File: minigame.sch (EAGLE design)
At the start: 44 parts, among them J1 AVR_SPI_PRG_6PTH, Q1 MMBT2222A, U1 MCP73831, U2 MIC5219 3.3V, Y1 8MHz

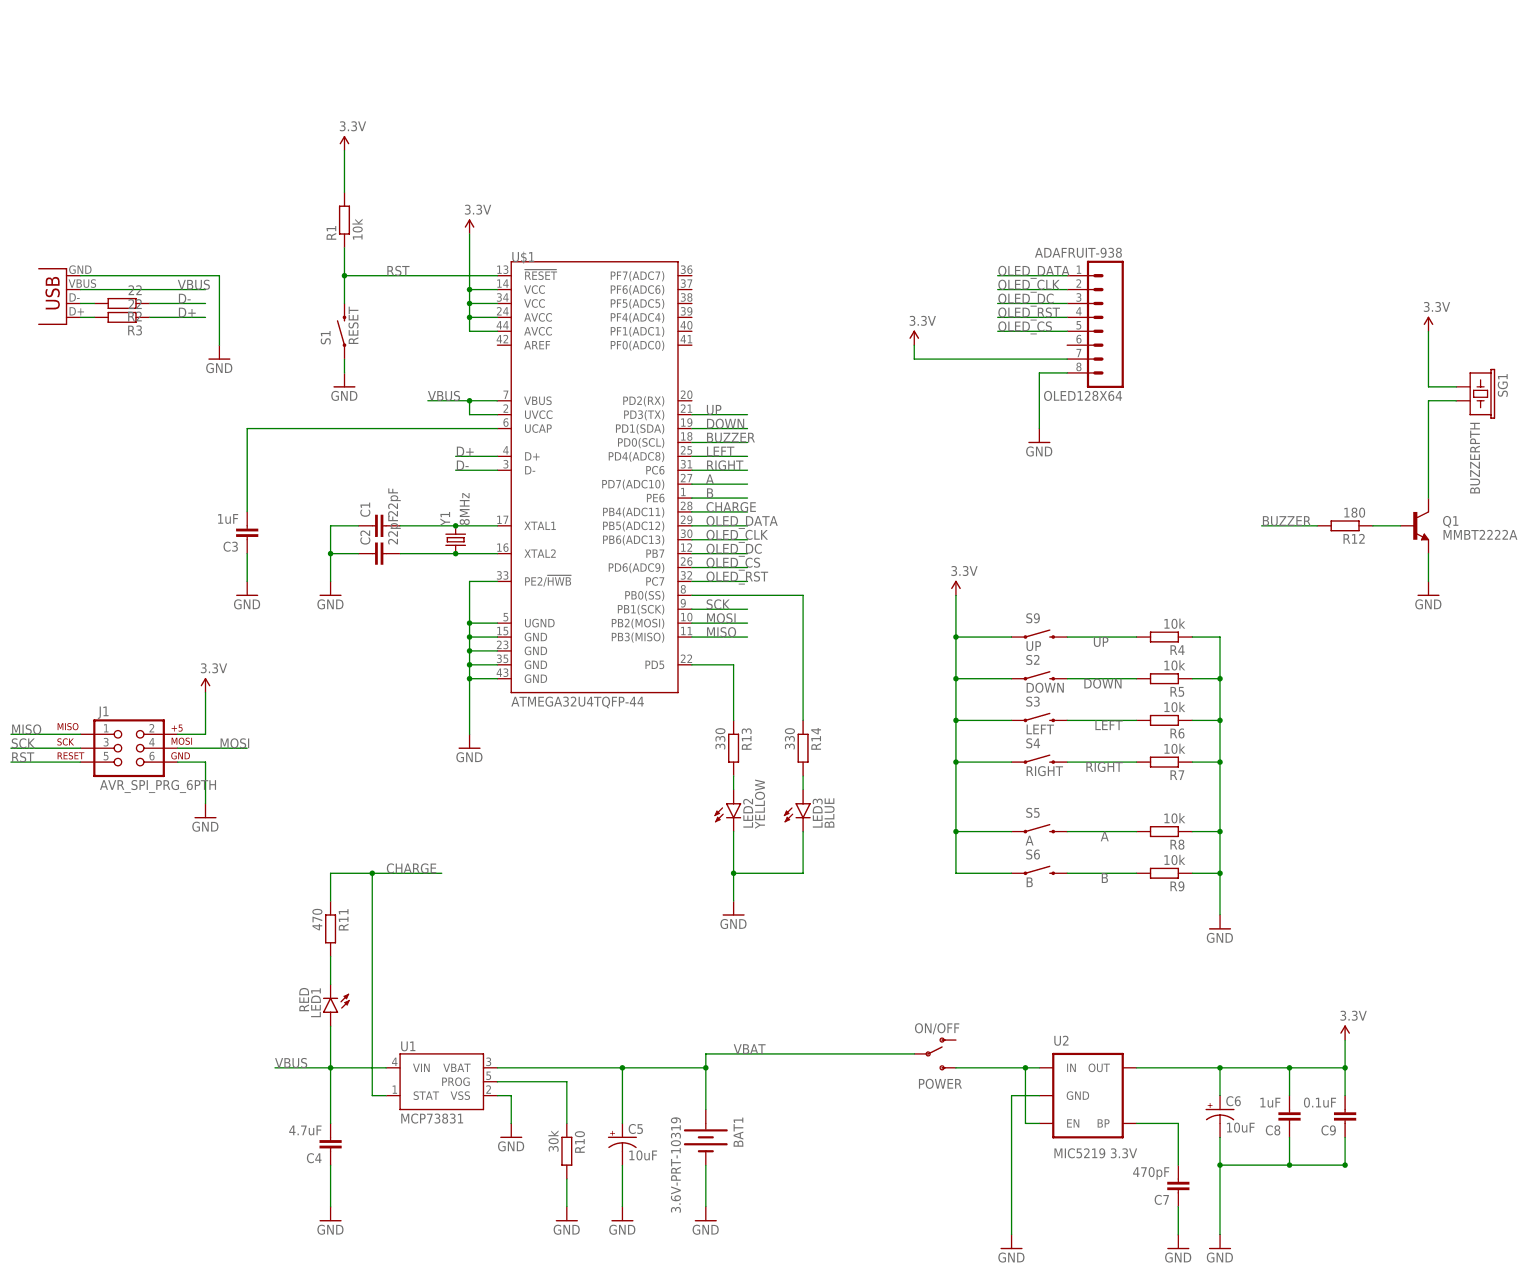
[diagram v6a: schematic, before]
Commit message: Voltage regulator removed Preliminary Routing test
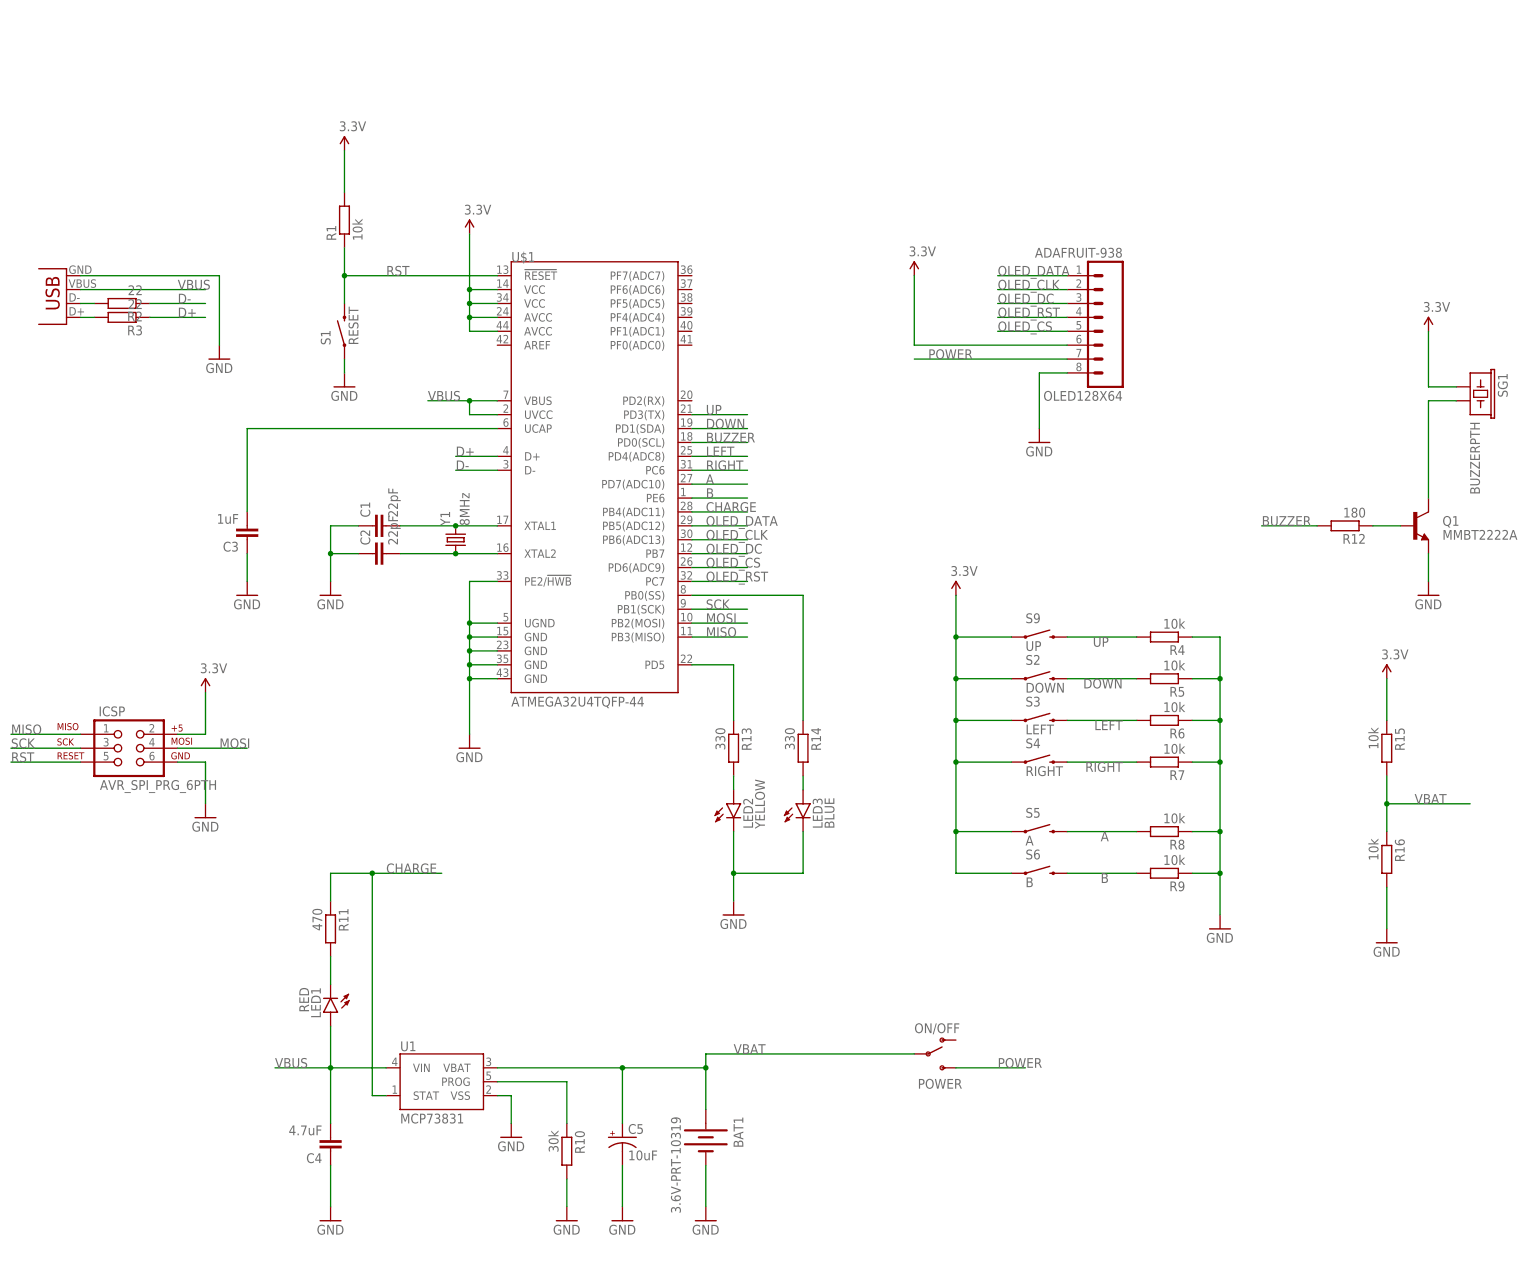
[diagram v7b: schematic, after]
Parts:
- removed C6: 10uF, SparkFun-Capacitors:CAP_POLD
- removed C7: 470pF, SparkFun-Passives:CAP1206
- removed C8: 1uF, SparkFun-Passives:CAP1206
- removed C9: 0.1uF, SparkFun-Passives:CAP1206
- removed U2: MIC5219 3.3V, SparkFun-PowerIC:V_REG_MIC52193.3V
- added R15, R16: 10k, rcl:R-EU_M0805
- renumbered J1 to ICSP
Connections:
- removed net N$10: POWER.S, U2.EN, U2.IN
- removed net N$8: C7.2, U2.BP
- new net POWER: OLED128X64.7, POWER.S
- net 3.3V: now also OLED128X64.6, R15.1; no longer C6.+, C8.2, C9.2, OLED128X64.7, U2.OUT
- net GND: now also R16.2; no longer C6.-, C7.1, C8.1, C9.1, U2.GND
- net VBAT: now also R15.2, R16.1

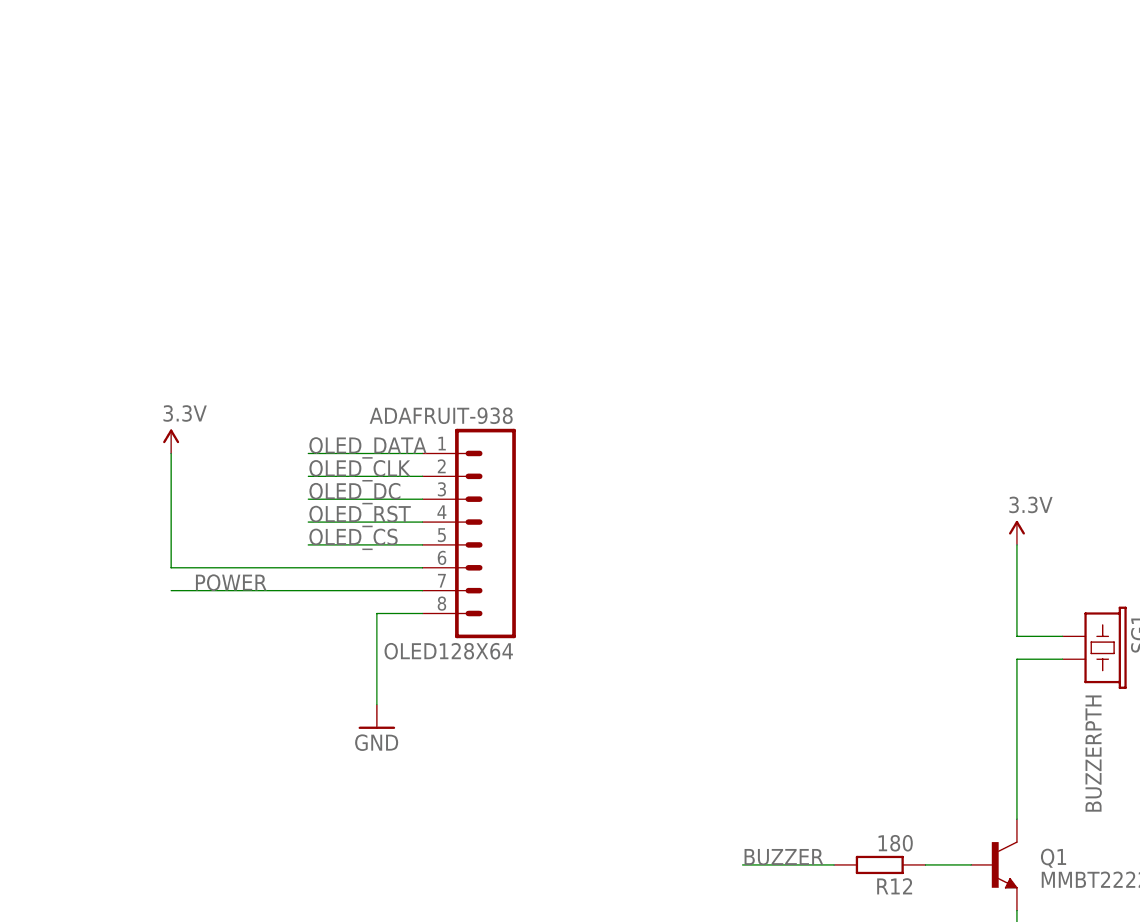
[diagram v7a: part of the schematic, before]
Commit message: Added new custom package for OLED display Updated schematic
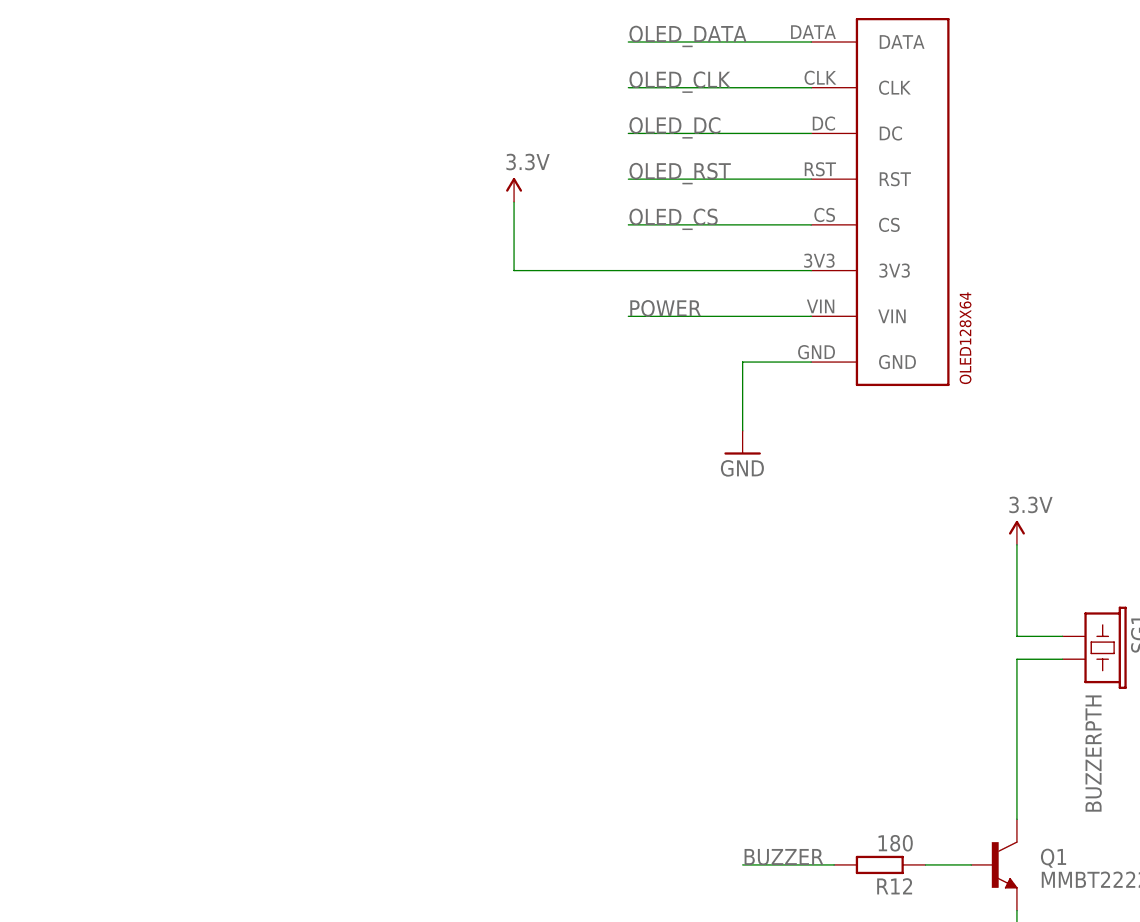
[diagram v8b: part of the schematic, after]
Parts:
- OLED128X64: value ADAFRUIT-938 -> OLED128X64-ADAFRUIT938; device SparkFun-Connectors:M08LONGPADS -> oled-128x64-adafruit-938:OLED128X64-ADAFRUIT938
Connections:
- net 3.3V: now also OLED128X64.3V3; no longer OLED128X64.6
- net GND: now also OLED128X64.GND; no longer OLED128X64.8
- net OLED_CLK: now also OLED128X64.CLK; no longer OLED128X64.2
- net OLED_CS: now also OLED128X64.CS; no longer OLED128X64.5
- net OLED_DATA: now also OLED128X64.DATA; no longer OLED128X64.1
- net OLED_DC: now also OLED128X64.DC; no longer OLED128X64.3
- net OLED_RST: now also OLED128X64.RST; no longer OLED128X64.4
- net POWER: now also OLED128X64.VIN; no longer OLED128X64.7
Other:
- moved on the sheet: OLED128X64
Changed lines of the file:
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@@
 <part name="SUPPLY3" library="SparkFun-Aesthetics" deviceset="3.3V" device=""/>
 <part name="LED1" library="SparkFun-LED" deviceset="LED" device="0603" value="RED"/>
-<part name="OLED128X64" library="SparkFun-Connectors" deviceset="M08" device="LONGPADS" value="ADAFRUIT-938"/>
 <part name="GND7" library="SparkFun-Aesthetics" deviceset="GND" device=""/>
 <part name="R4" library="rcl" deviceset="R-EU_" device="M0805" value="10k"/>
@@
 <part name="R11" library="rcl" deviceset="R-EU_" device="M0805" value="470"/>
 <part name="GND12" library="SparkFun-Aesthetics" deviceset="GND" device=""/>
-<part name="COPY+1" library="SparkFun-Aesthetics" deviceset="GND" device=""/>
 <part name="SG1" library="SparkFun-Electromechanical" deviceset="BUZZER" device="PTH"/>
 <part name="Q1" library="SparkFun-DiscreteSemi" deviceset="TRANSISTOR_NPN" device="MMBT2222A" value="MMBT2222A"/>
@@
 <part name="R14" library="rcl" deviceset="R-EU_" device="M0805" value="330"/>
 <part name="GND1" library="SparkFun-Aesthetics" deviceset="GND" device=""/>
-<part name="SUPPLY5" library="SparkFun-Aesthetics" deviceset="3.3V" device=""/>
 <part name="R15" library="rcl" deviceset="R-EU_" device="M0805" value="10k"/>
 <part name="R16" library="rcl" deviceset="R-EU_" device="M0805" value="10k"/>
 <part name="GND13" library="SparkFun-Aesthetics" deviceset="GND" device=""/>
 <part name="SUPPLY6" library="SparkFun-Aesthetics" deviceset="3.3V" device=""/>
+<part name="OLED128X64" library="oled-128x64-adafruit-938" deviceset="OLED128X64-ADAFRUIT938" device=""/>
+<part name="COPY+3" library="SparkFun-Aesthetics" deviceset="GND" device=""/>
+<part name="SUPPLY8" library="SparkFun-Aesthetics" deviceset="3.3V" device=""/>
 </parts>
 <sheets>
@@
 <instance part="SUPPLY3" gate="G$1" x="-55.88" y="0"/>
 <instance part="LED1" gate="G$1" x="-33.02" y="-58.42" rot="R180"/>
-<instance part="OLED128X64" gate="G$1" x="106.68" y="68.58" rot="R180"/>
 <instance part="GND7" gate="1" x="129.54" y="-43.18"/>
 <instance part="R4" gate="G$1" x="119.38" y="10.16" rot="R180"/>
@@
 <instance part="R11" gate="G$1" x="-33.02" y="-43.18" rot="R270"/>
 <instance part="GND12" gate="1" x="-33.02" y="-96.52"/>
-<instance part="COPY+1" gate="1" x="96.52" y="45.72"/>
 <instance part="SG1" gate="G$1" x="175.26" y="55.88" rot="R270"/>
 <instance part="Q1" gate="G$1" x="165.1" y="30.48"/>
@@
 <instance part="R14" gate="G$1" x="53.34" y="-10.16" rot="R270"/>
 <instance part="GND1" gate="1" x="40.64" y="-40.64"/>
-<instance part="SUPPLY5" gate="G$1" x="73.66" y="76.2"/>
 <instance part="R15" gate="G$1" x="160.02" y="-10.16" rot="R270"/>
 <instance part="R16" gate="G$1" x="160.02" y="-30.48" rot="R270"/>
 <instance part="GND13" gate="1" x="160.02" y="-45.72"/>
 <instance part="SUPPLY6" gate="G$1" x="160.02" y="2.54"/>
+<instance part="OLED128X64" gate="G$1" x="154.94" y="109.22"/>
+<instance part="COPY+3" gate="1" x="137.16" y="76.2"/>
+<instance part="SUPPLY8" gate="G$1" x="111.76" y="104.14"/>
 </instances>
 <busses>
@@
 </segment>
 <segment>
-<pinref part="COPY+1" gate="1" pin="GND"/>
-<wire x1="96.52" y1="48.26" x2="96.52" y2="58.42" width="0.1524" layer="91"/>
-<pinref part="OLED128X64" gate="G$1" pin="8"/>
-<wire x1="96.52" y1="58.42" x2="101.6" y2="58.42" width="0.1524" layer="91"/>
-</segment>
-<segment>
 <pinref part="COPY+2" gate="1" pin="GND"/>
 <pinref part="Q1" gate="G$1" pin="E"/>
@@
 <pinref part="GND13" gate="1" pin="GND"/>
 <wire x1="160.02" y1="-35.56" x2="160.02" y2="-43.18" width="0.1524" layer="91"/>
+</segment>
+<segment>
+<pinref part="OLED128X64" gate="G$1" pin="GND"/>
+<pinref part="COPY+3" gate="1" pin="GND"/>
+<wire x1="144.78" y1="86.36" x2="137.16" y2="86.36" width="0.1524" layer="91"/>
+<wire x1="137.16" y1="86.36" x2="137.16" y2="78.74" width="0.1524" layer="91"/>
 </segment>
 </net>
@@
 </segment>
 <segment>
-<pinref part="OLED128X64" gate="G$1" pin="6"/>
-<wire x1="101.6" y1="63.5" x2="73.66" y2="63.5" width="0.1524" layer="91"/>
-<wire x1="73.66" y1="63.5" x2="73.66" y2="76.2" width="0.1524" layer="91"/>
-<pinref part="SUPPLY5" gate="G$1" pin="3.3V"/>
-</segment>
-<segment>
 <pinref part="SUPPLY6" gate="G$1" pin="3.3V"/>
 <pinref part="R15" gate="G$1" pin="1"/>
 <wire x1="160.02" y1="2.54" x2="160.02" y2="-5.08" width="0.1524" layer="91"/>
+</segment>
+<segment>
+<pinref part="OLED128X64" gate="G$1" pin="3V3"/>
+<pinref part="SUPPLY8" gate="G$1" pin="3.3V"/>
+<wire x1="144.78" y1="96.52" x2="111.76" y2="96.52" width="0.1524" layer="91"/>
+<wire x1="111.76" y1="96.52" x2="111.76" y2="104.14" width="0.1524" layer="91"/>
 </segment>
 </net>
@@
 <net name="OLED_DATA" class="0">
 <segment>
-<pinref part="OLED128X64" gate="G$1" pin="1"/>
-<wire x1="101.6" y1="76.2" x2="88.9" y2="76.2" width="0.1524" layer="91"/>
-<label x="88.9" y="76.2" size="1.778" layer="95"/>
-</segment>
-<segment>
 <pinref part="U$1" gate="G$1" pin="PB5(ADC12)"/>
 <wire x1="33.02" y1="30.48" x2="43.18" y2="30.48" width="0.1524" layer="91"/>
 <label x="35.56" y="30.48" size="1.778" layer="95"/>
 </segment>
+<segment>
+<pinref part="OLED128X64" gate="G$1" pin="DATA"/>
+<wire x1="144.78" y1="121.92" x2="124.46" y2="121.92" width="0.1524" layer="91"/>
+<label x="124.46" y="121.92" size="1.778" layer="95"/>
+</segment>
 </net>
 <net name="OLED_CLK" class="0">
-<segment>
-<pinref part="OLED128X64" gate="G$1" pin="2"/>
-<wire x1="101.6" y1="73.66" x2="88.9" y2="73.66" width="0.1524" layer="91"/>
-<label x="88.9" y="73.66" size="1.778" layer="95"/>
-</segment>
 <segment>
 <pinref part="U$1" gate="G$1" pin="PB6(ADC13)"/>
@@
 <label x="35.56" y="27.94" size="1.778" layer="95"/>
 </segment>
+<segment>
+<pinref part="OLED128X64" gate="G$1" pin="CLK"/>
+<wire x1="144.78" y1="116.84" x2="124.46" y2="116.84" width="0.1524" layer="91"/>
+<label x="124.46" y="116.84" size="1.778" layer="95"/>
+</segment>
 </net>
 <net name="OLED_DC" class="0">
-<segment>
-<pinref part="OLED128X64" gate="G$1" pin="3"/>
-<wire x1="101.6" y1="71.12" x2="88.9" y2="71.12" width="0.1524" layer="91"/>
-<label x="88.9" y="71.12" size="1.778" layer="95"/>
-</segment>
 <segment>
 <pinref part="U$1" gate="G$1" pin="PB7"/>
@@
 <label x="35.56" y="25.4" size="1.778" layer="95"/>
 </segment>
+<segment>
+<pinref part="OLED128X64" gate="G$1" pin="DC"/>
+<wire x1="144.78" y1="111.76" x2="124.46" y2="111.76" width="0.1524" layer="91"/>
+<label x="124.46" y="111.76" size="1.778" layer="95"/>
+</segment>
 </net>
 <net name="OLED_RST" class="0">
-<segment>
-<pinref part="OLED128X64" gate="G$1" pin="4"/>
-<wire x1="101.6" y1="68.58" x2="88.9" y2="68.58" width="0.1524" layer="91"/>
-<label x="88.9" y="68.58" size="1.778" layer="95"/>
-</segment>
 <segment>
 <pinref part="U$1" gate="G$1" pin="PC7"/>
@@
 <label x="35.56" y="20.32" size="1.778" layer="95"/>
 </segment>
+<segment>
+<pinref part="OLED128X64" gate="G$1" pin="RST"/>
+<wire x1="144.78" y1="106.68" x2="124.46" y2="106.68" width="0.1524" layer="91"/>
+<label x="124.46" y="106.68" size="1.778" layer="95"/>
+</segment>
 </net>
 <net name="OLED_CS" class="0">
-<segment>
-<pinref part="OLED128X64" gate="G$1" pin="5"/>
-<wire x1="101.6" y1="66.04" x2="88.9" y2="66.04" width="0.1524" layer="91"/>
-<label x="88.9" y="66.04" size="1.778" layer="95"/>
-</segment>
 <segment>
 <pinref part="U$1" gate="G$1" pin="PD6(ADC9)"/>
 <wire x1="33.02" y1="22.86" x2="43.18" y2="22.86" width="0.1524" layer="91"/>
 <label x="35.56" y="22.86" size="1.778" layer="95"/>
+</segment>
+<segment>
+<pinref part="OLED128X64" gate="G$1" pin="CS"/>
+<wire x1="144.78" y1="101.6" x2="124.46" y2="101.6" width="0.1524" layer="91"/>
+<label x="124.46" y="101.6" size="1.778" layer="95"/>
 </segment>
 </net>
@@
 </segment>
 <segment>
-<pinref part="OLED128X64" gate="G$1" pin="7"/>
-<wire x1="101.6" y1="60.96" x2="73.66" y2="60.96" width="0.1524" layer="91"/>
-<label x="76.2" y="60.96" size="1.778" layer="95"/>
-</segment>
-</net>
+<pinref part="OLED128X64" gate="G$1" pin="VIN"/>
+<wire x1="144.78" y1="91.44" x2="124.46" y2="91.44" width="0.1524" layer="91"/>
+<label x="124.46" y="91.44" size="1.778" layer="95"/>
+</segment>
+</net>
